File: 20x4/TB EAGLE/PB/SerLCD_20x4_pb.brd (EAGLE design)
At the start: 101.6 x 165.1 mm, 24 parts, among them J1 AVR_PROG, J3 SER_LCD20X4, U1 5V Flying Jalapeno, U2 74LVC4066_MUX_1:1_X4

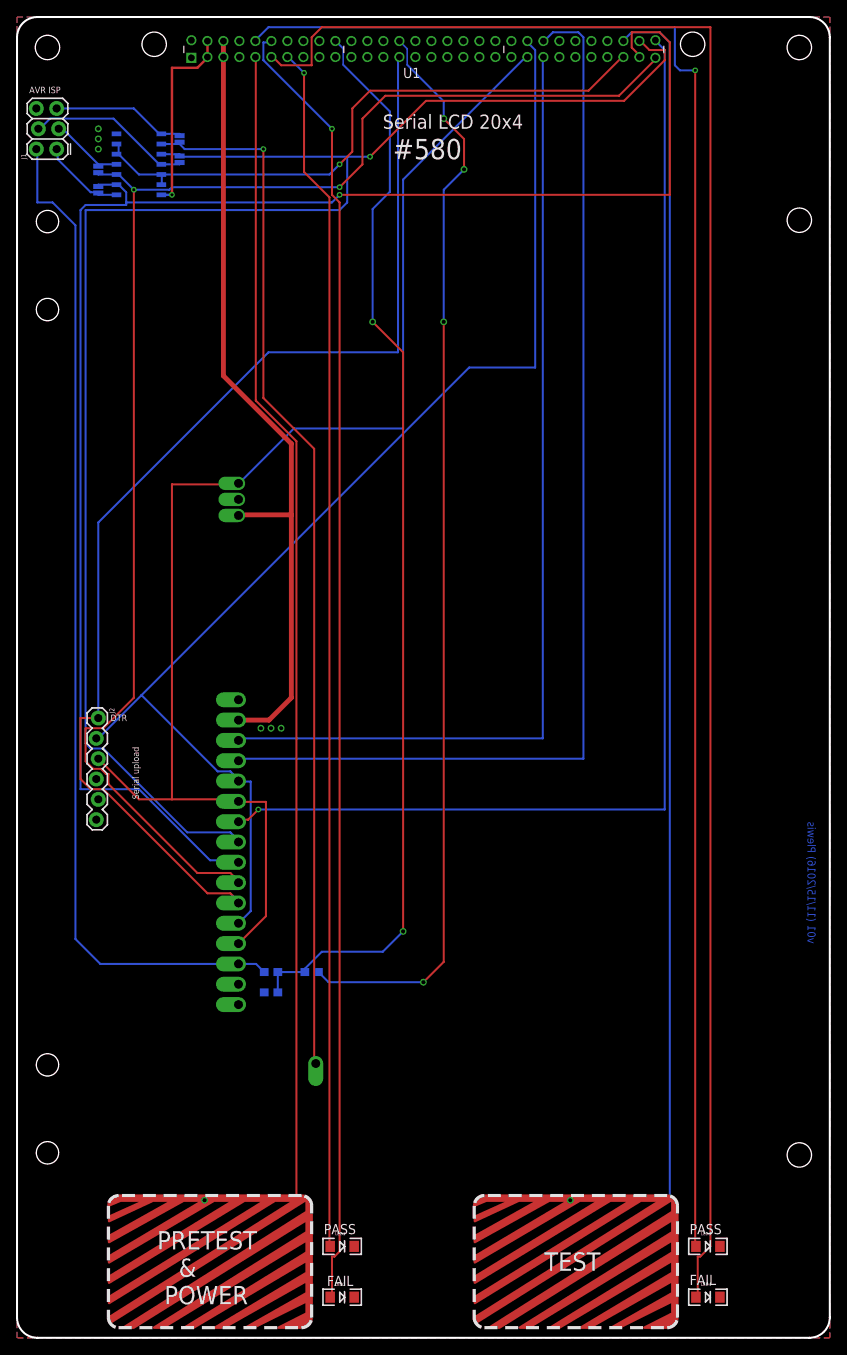
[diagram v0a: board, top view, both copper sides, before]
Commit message: 20x4 pb routing done
-changed switch to isolate FJ SPI lines (because the new pi_grammer has isolation built in)
-added more support beam standoffs
-moved to new FJ footprint for easier assembly on RA 2x30 header.
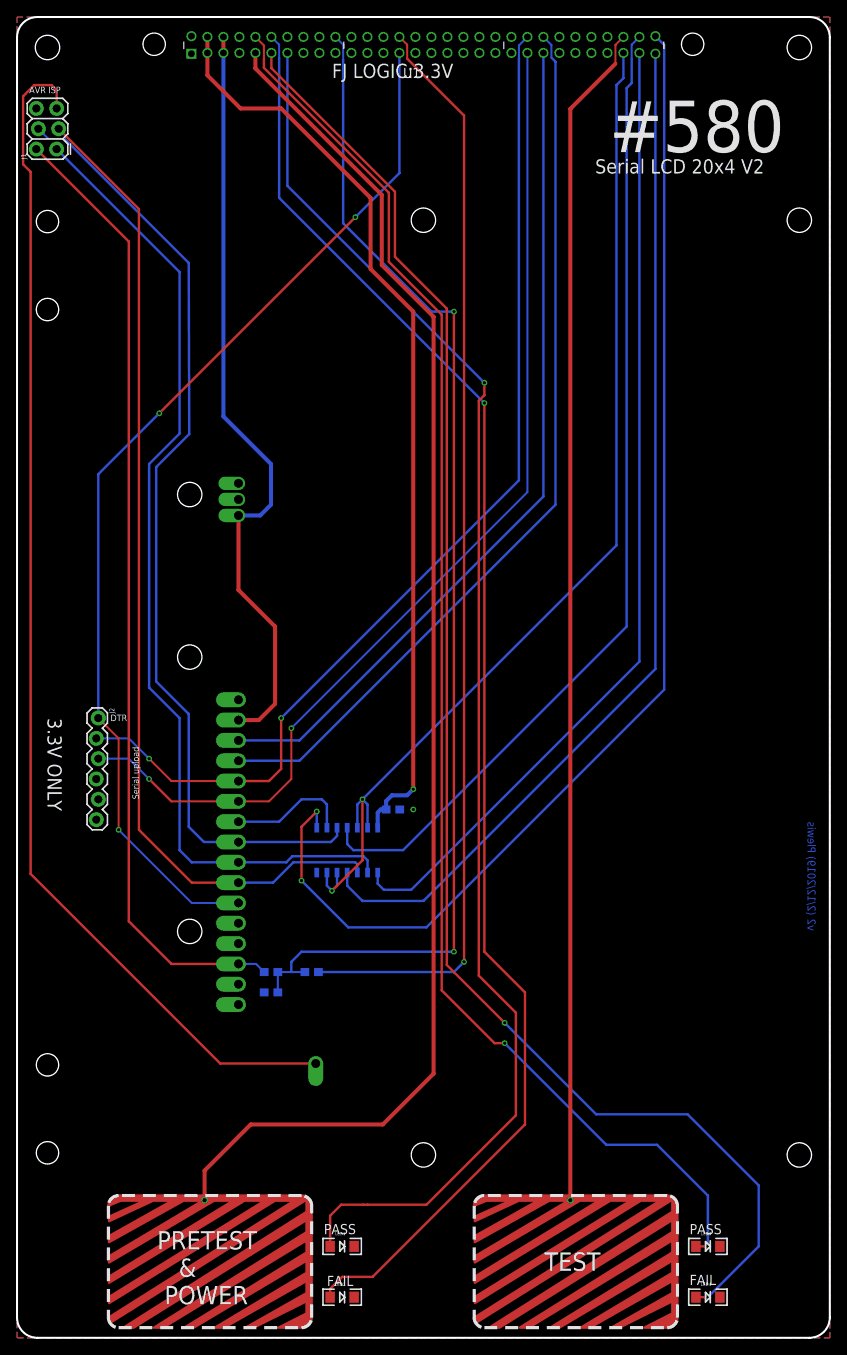
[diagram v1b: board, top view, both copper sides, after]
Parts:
- removed JP1: MISO, SparkFun-Jumpers:SMT-JUMPER_2_NC_PASTE_NO-SILK
- removed JP2: SCK, SparkFun-Jumpers:SMT-JUMPER_2_NC_PASTE_NO-SILK
- removed JP3: RST, SparkFun-Jumpers:SMT-JUMPER_2_NC_PASTE_NO-SILK
- removed JP4: MOSI, SparkFun-Jumpers:SMT-JUMPER_2_NC_PASTE_NO-SILK
- added C1: 0.1uF, Testing:0603-CAP
- added U$10, U$11, U$4, U$5, U$9: (no value), SparkFun:STAND-OFF-TIGHT
- U1: device Testing:FLYING_JALAPENO_V2_M -> Testing:FLYING_JALAPENO_V3_1_M
- moved U2 89.2 mm to (41.9, 61.0), turned to 0 degrees
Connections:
- net PGM_SWITCH_EN renamed SPI_FJ_SWITCH_EN
- removed net MISO_P: J1.1, JP1.1, U2.1
- removed net MOSI_P: J1.4, JP4.1, U2.11
- removed net RST_P: J1.5, JP3.1, U2.8
- removed net SCK_P: J1.3, JP2.1, U2.4
- new net CS_FJ: U1.60, U2.8
- new net MISO_FJ: U1.29, U2.1
- new net MOSI_FJ: U1.59, U2.11
- new net SCK_FJ: U1.30, U2.4
- net 5V_VIN: now also C1.1
- net CS: now also U2.9; no longer U1.60
- net GND: now also C1.2
- net MISO: now also J1.1; no longer JP1.2, U1.29
- net MOSI: now also J1.4; no longer JP4.2, U1.59
- net RST: now also J1.5; no longer JP3.2, U2.9
- net RX1_FJ: no longer J3.P$5
- net SCK: now also J1.3; no longer JP2.2, U1.30
- net TX1_FJ: no longer J3.P$19, J3.P$4
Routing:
- net CS_FJ: track 0.00 -> 153.7 mm, vias 0 -> 2
- net CS: track 150.5 -> 15.4 mm, vias 1 -> 0
- net SCK_FJ: track 0.00 -> 129.9 mm
- net MOSI_FJ: track 0.00 -> 123.2 mm
- net MISO_FJ: track 0.00 -> 122.3 mm
- net 5V_VIN: track 24.3 -> 115.8 mm
- net MOSI: track 202.9 -> 120.3 mm, vias 1 -> 0
- net MISO: track 203.9 -> 123.3 mm, vias 1 -> 0
- net SCK: track 182.4 -> 124.0 mm, vias 2 -> 0
- net SPI_FJ_SWITCH_EN: track 76.5 -> 132.5 mm, vias 1 -> 2
- net TX1_FJ: track 166.5 -> 130.5 mm, vias 0 -> 2
- net N$6: track 219.1 -> 191.6 mm, vias 0 -> 2
- net N$5: track 207.9 -> 180.6 mm, vias 1 -> 2
- net SCL: track 139.1 -> 112.0 mm
- net N$3: track 151.0 -> 177.5 mm
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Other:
- board text added: "0.1uF"
- board text added: "3.3V ONLY"
- board text added: "FJ LOGIC:3.3V"
- board text added: "Serial LCD 20x4 V2"
- board text added: "v2 (2/12/2019) Plewis"
- board text removed: "Serial LCD 20x4"
- board text removed: "v01 (11/15/2016) Plewis"

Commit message: 20x4 testbed PB updated for new qwiic connector version
-also removed old PM footprints, cuz these aren't used in making acrylic layers anyways, and they are now out of date with pogopin spacing.
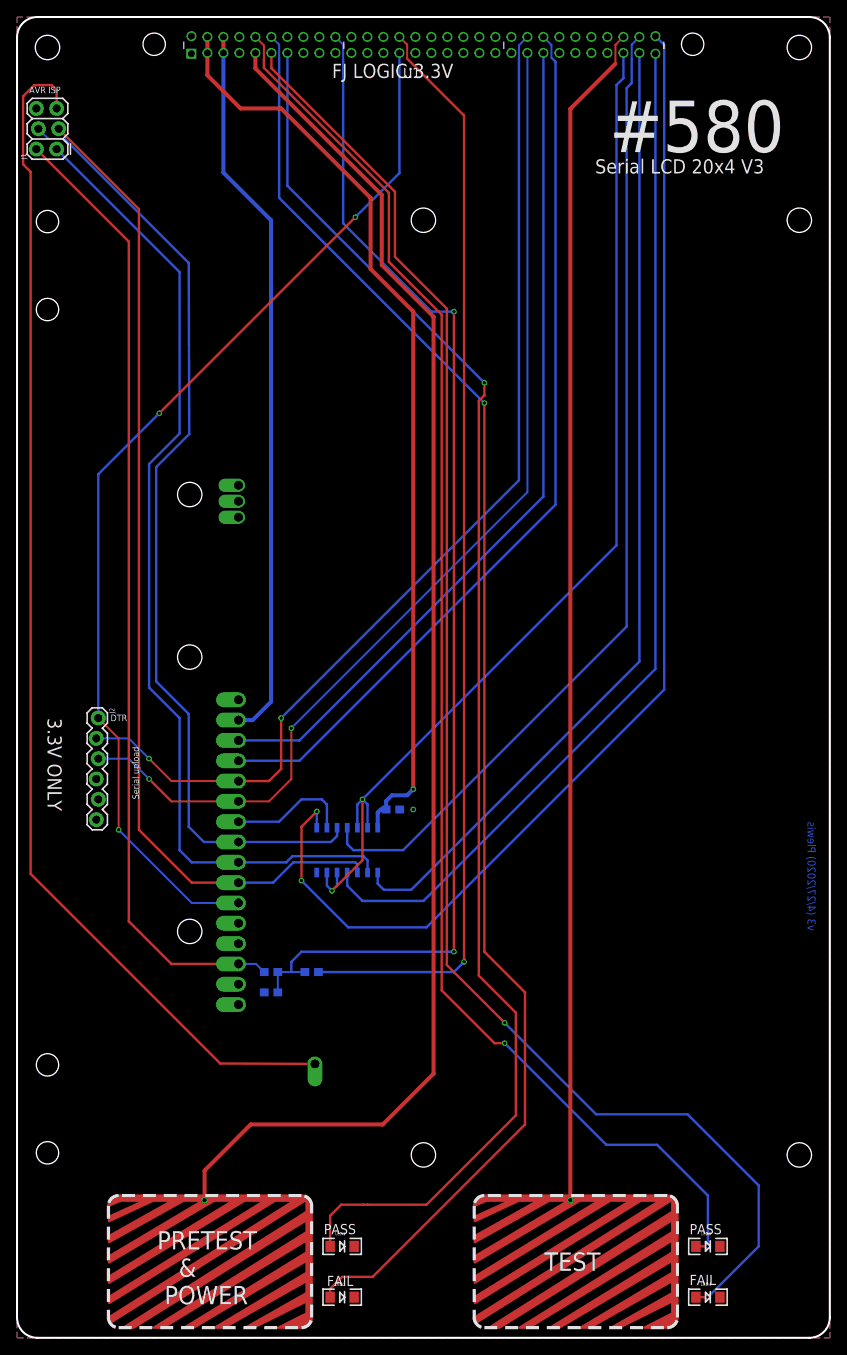
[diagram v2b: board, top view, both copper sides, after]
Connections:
- net GND: no longer J3.P$18
- net RAW_VIA_V2: no longer J3.P$17
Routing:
- net RAW_VIA_V2: track 96.4 -> 90.6 mm
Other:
- board text added: "Serial LCD 20x4 V3"
- board text added: "v3 (4/27/2020) Plewis"
- board text removed: "Serial LCD 20x4 V2"
- board text removed: "v2 (2/12/2019) Plewis"
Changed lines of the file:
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@@
 <?xml version="1.0" encoding="utf-8"?>
 <!DOCTYPE eagle SYSTEM "eagle.dtd">
-<eagle version="9.2.2">
+<eagle version="9.5.2">
 <drawing>
 <settings>
@@
 <wire x1="99.06" y1="143.51" x2="1.27" y2="143.51" width="0.254" layer="49"/>
 <wire x1="1.27" y1="143.51" x2="0" y2="140.97" width="0.254" layer="49" curve="90"/>
-<text x="72.263" y="145.542" size="1.778" layer="21" font="vector" ratio="15">Serial LCD 20x4 V2</text>
-<text x="99.822" y="64.516" size="1.016" layer="16" font="vector" ratio="15" rot="MR270">v2 (2/12/2019) Plewis</text>
+<text x="72.263" y="145.542" size="1.778" layer="21" font="vector" ratio="15">Serial LCD 20x4 V3</text>
+<text x="99.822" y="64.516" size="1.016" layer="16" font="vector" ratio="15" rot="MR270">v3 (4/27/2020) Plewis</text>
 <text x="17.526" y="4.191" size="2.286" layer="21" font="vector" ratio="15">PRETEST
    &amp;
@@
 <contactref element="J3" pad="P$1"/>
 <contactref element="J3" pad="P$2"/>
-<contactref element="J3" pad="P$18"/>
 <contactref element="J1" pad="6"/>
 <contactref element="J2" pad="6"/>
@@
 <contactref element="U1" pad="33"/>
 <contactref element="U1" pad="3"/>
-<contactref element="J3" pad="P$17"/>
 <contactref element="J3" pad="P$15"/>
 <wire x1="25.8" y1="162.608" x2="25.8" y2="160.608" width="0.508" layer="1"/>
-<wire x1="25.8" y1="160.608" x2="25.8" y2="115.17" width="0.508" layer="16"/>
-<wire x1="25.8" y1="115.17" x2="31.75" y2="109.22" width="0.508" layer="16"/>
-<wire x1="31.75" y1="109.22" x2="31.75" y2="104.14" width="0.508" layer="16"/>
-<wire x1="31.75" y1="104.14" x2="30.4038" y2="102.7938" width="0.508" layer="16"/>
-<wire x1="30.4038" y1="102.7938" x2="27.686" y2="102.7938" width="0.508" layer="16"/>
-<wire x1="27.686" y1="102.7938" x2="27.686" y2="93.472" width="0.508" layer="1"/>
-<wire x1="27.686" y1="93.472" x2="32.258" y2="88.9" width="0.508" layer="1"/>
-<wire x1="32.258" y1="88.9" x2="32.258" y2="79.248" width="0.508" layer="1"/>
-<wire x1="30.226" y1="77.216" x2="27.686" y2="77.216" width="0.508" layer="1"/>
-<wire x1="32.258" y1="79.248" x2="30.226" y2="77.216" width="0.508" layer="1"/>
+<wire x1="25.8" y1="160.608" x2="25.8" y2="145.65" width="0.508" layer="16"/>
+<wire x1="25.8" y1="145.65" x2="31.75" y2="139.7" width="0.508" layer="16"/>
+<wire x1="29.464" y1="77.216" x2="27.686" y2="77.216" width="0.508" layer="16"/>
+<wire x1="31.75" y1="139.7" x2="31.75" y2="79.502" width="0.508" layer="16"/>
+<wire x1="31.75" y1="79.502" x2="29.464" y2="77.216" width="0.508" layer="16"/>
 </signal>
 <signal name="MISO">
@@
 <contactref element="J3" pad="P$20"/>
 <contactref element="J1" pad="5"/>
-<wire x1="37.338" y1="34.29" x2="25.4" y2="34.29" width="0.3048" layer="1"/>
+<wire x1="37.2364" y1="34.2392" x2="25.4" y2="34.29" width="0.3048" layer="1"/>
 <wire x1="1.7018" y1="57.9882" x2="25.4" y2="34.29" width="0.3048" layer="1"/>
 <wire x1="0.762" y1="155.194" x2="0.762" y2="146.685" width="0.3048" layer="1"/>
